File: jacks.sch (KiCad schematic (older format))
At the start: 71 parts, among them Q601 MMBT3904, Q602 MMBT3904, Q603 MMBT3904, Q604 MMBT3904, U601 MCP6004, U602 6N137

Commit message: only ground plane left
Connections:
- net GND: now also CVIN1.2, CVIN2.2, CVIN3.2, CVIN4.2
- no-connect marks 24 -> 20

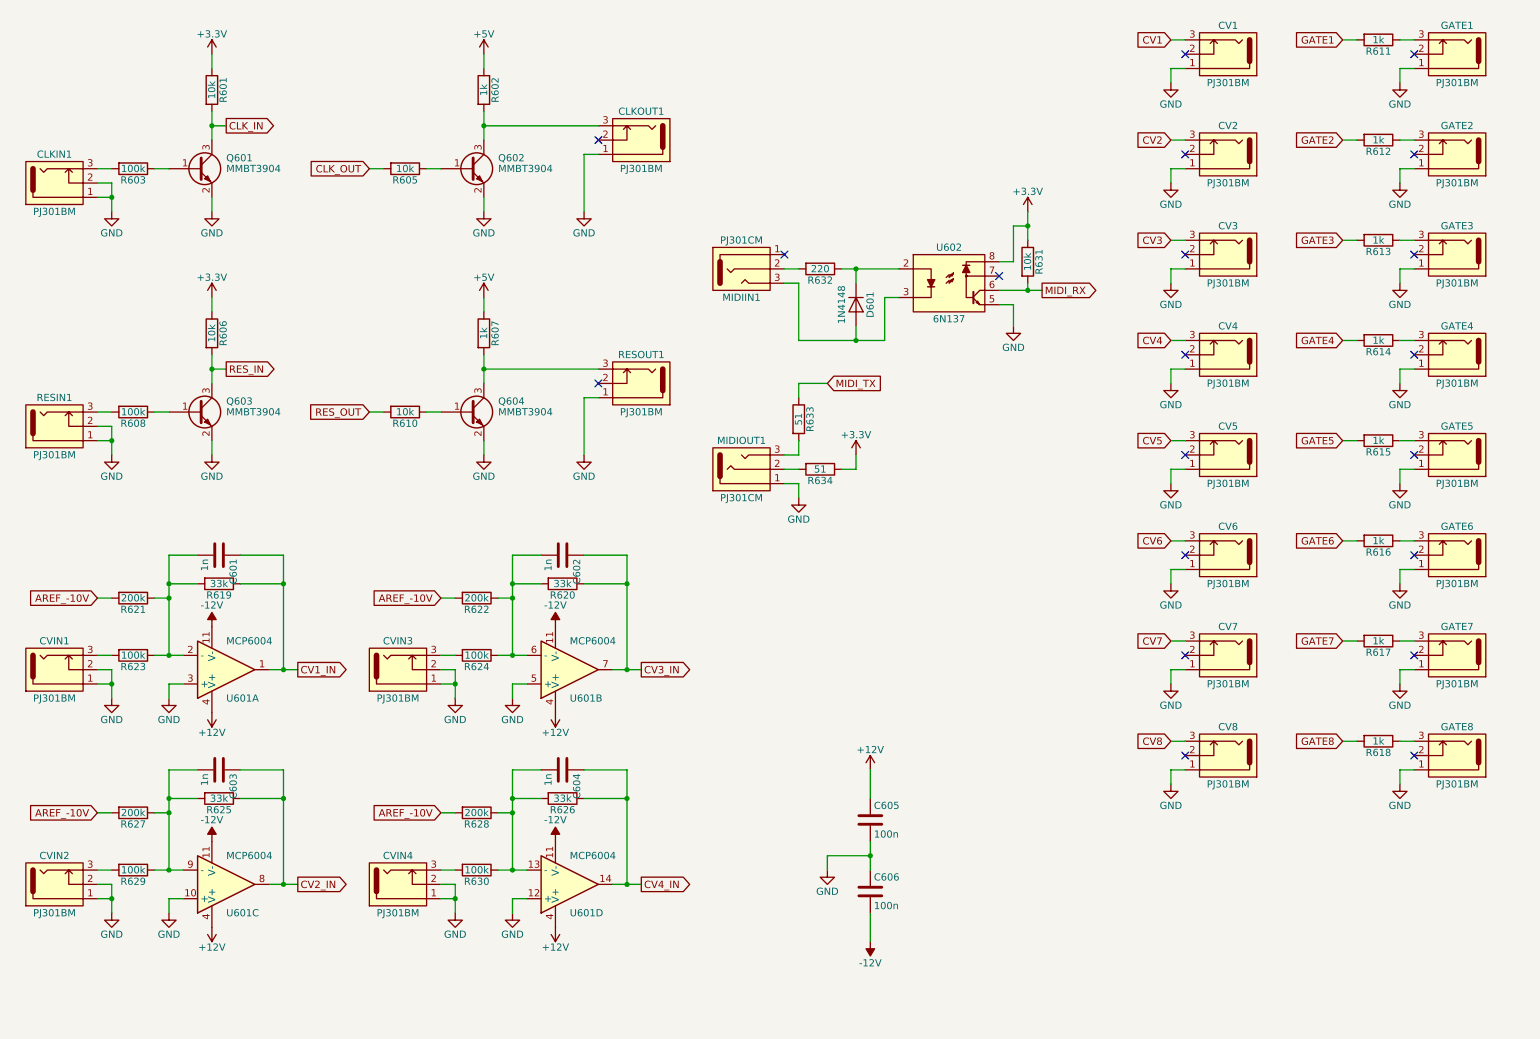
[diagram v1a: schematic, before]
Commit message: renamed jacks
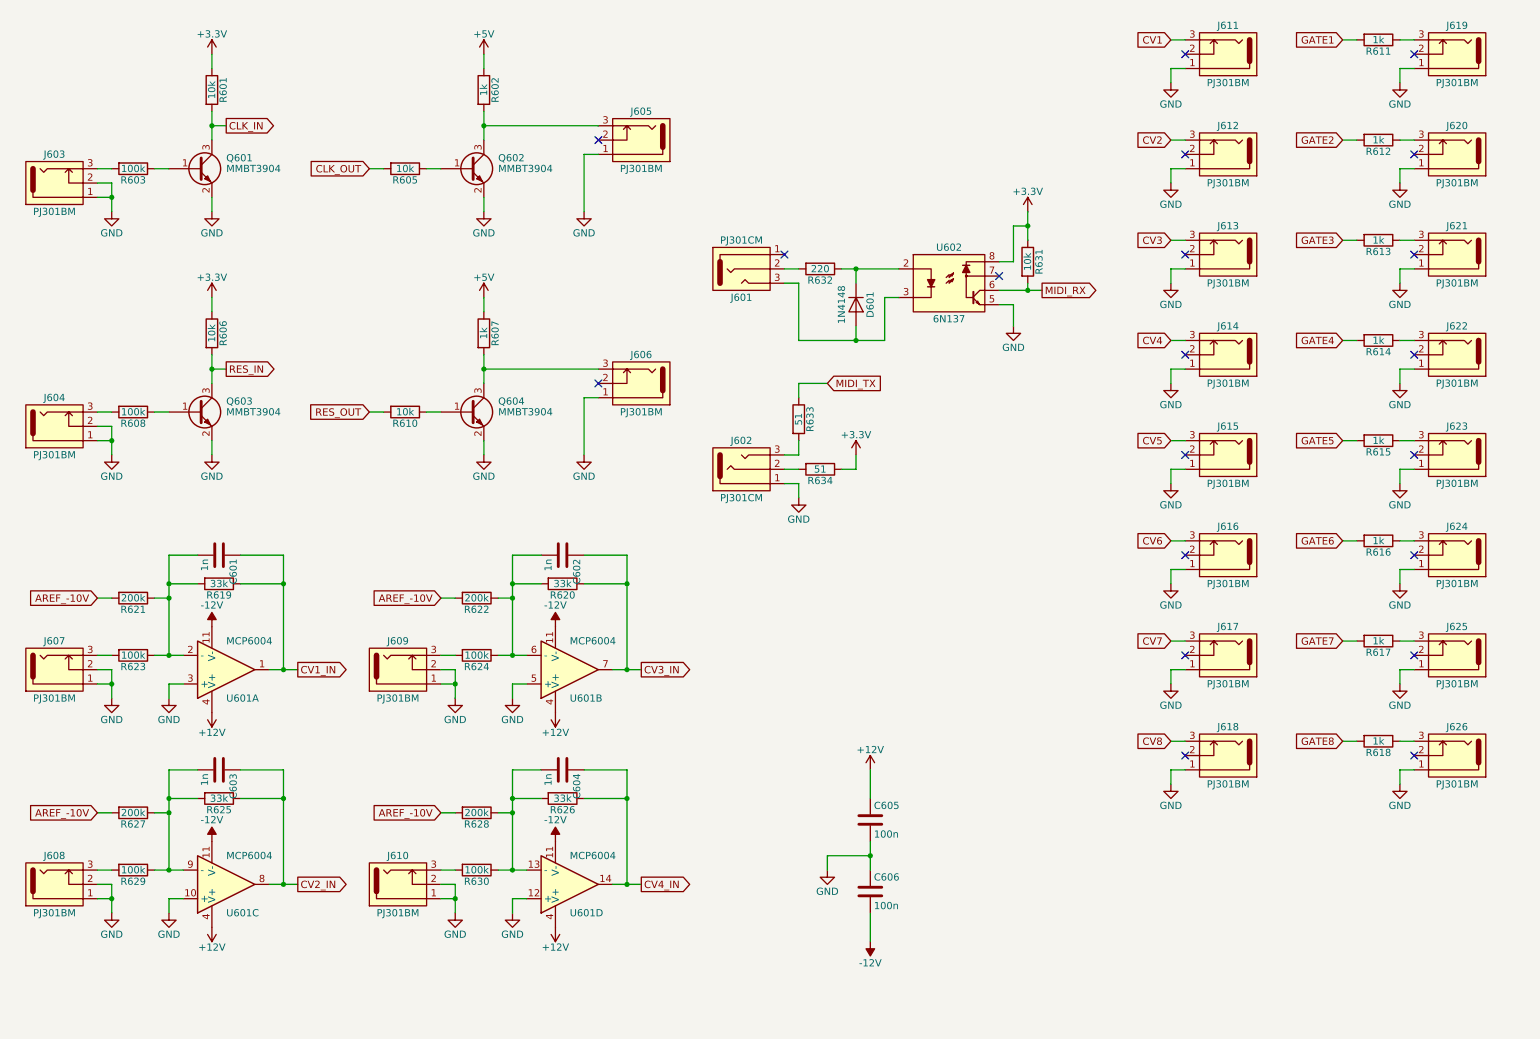
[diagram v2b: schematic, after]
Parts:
- renumbered MIDIIN1 to J601, MIDIOUT1 to J602, CLKIN1 to J603, RESIN1 to J604, CLKOUT1 to J605, RESOUT1 to J606, CVIN1 to J607, CVIN2 to J608, CVIN3 to J609, CVIN4 to J610, CV1 to J611, CV2 to J612, CV3 to J613, CV4 to J614, CV5 to J615, CV6 to J616, CV7 to J617, CV8 to J618, GATE1 to J619, GATE2 to J620, GATE3 to J621, GATE4 to J622, GATE5 to J623, GATE6 to J624, GATE7 to J625, GATE8 to J626
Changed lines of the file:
@@
 $EndComp
 $Comp
-L PJ301BM CLKIN1
+L PJ301BM J603
 U 1 1 59D9587D
 P 1000 1800
-F 0 "CLKIN1" H 800 1600 50  0000 C CNN
+F 0 "J603" H 800 1600 50  0000 C CNN
 F 1 "PJ301BM" H 800 2000 50  0000 C CNN
 F 2 "w_connector:PJ301BM" H 1150 1900 50  0001 C CNN
@@
 $EndComp
 $Comp
-L PJ301BM RESIN1
+L PJ301BM J604
 U 1 1 59D95DE7
 P 1000 3500
-F 0 "RESIN1" H 800 3300 50  0000 C CNN
+F 0 "J604" H 800 3300 50  0000 C CNN
 F 1 "PJ301BM" H 800 3700 50  0000 C CNN
 F 2 "w_connector:PJ301BM" H 1150 3600 50  0001 C CNN
@@
 $EndComp
 $Comp
-L PJ301BM CLKOUT1
+L PJ301BM J605
 U 1 1 59D96412
 P 4700 1500
-F 0 "CLKOUT1" H 4500 1300 50  0000 C CNN
+F 0 "J605" H 4500 1300 50  0000 C CNN
 F 1 "PJ301BM" H 4500 1700 50  0000 C CNN
 F 2 "w_connector:PJ301BM" H 4850 1600 50  0001 C CNN
@@
 $EndComp
 $Comp
-L PJ301BM RESOUT1
+L PJ301BM J606
 U 1 1 59D970A1
 P 4700 3200
-F 0 "RESOUT1" H 4500 3000 50  0000 C CNN
+F 0 "J606" H 4500 3000 50  0000 C CNN
 F 1 "PJ301BM" H 4500 3400 50  0000 C CNN
 F 2 "w_connector:PJ301BM" H 4850 3300 50  0001 C CNN
@@
 $EndComp
 $Comp
-L PJ301BM CV1
+L PJ301BM J611
 U 1 1 59D98BF9
 P 8800 900
-F 0 "CV1" H 8600 700 50  0000 C CNN
+F 0 "J611" H 8600 700 50  0000 C CNN
 F 1 "PJ301BM" H 8600 1100 50  0000 C CNN
 F 2 "w_connector:PJ301BM" H 8950 1000 50  0001 C CNN
@@
 $EndComp
 $Comp
-L PJ301BM CV2
+L PJ301BM J612
 U 1 1 59D99393
 P 8800 1600
-F 0 "CV2" H 8600 1400 50  0000 C CNN
+F 0 "J612" H 8600 1400 50  0000 C CNN
 F 1 "PJ301BM" H 8600 1800 50  0000 C CNN
 F 2 "w_connector:PJ301BM" H 8950 1700 50  0001 C CNN
@@
 $EndComp
 $Comp
-L PJ301BM CV3
+L PJ301BM J613
 U 1 1 59D99402
 P 8800 2300
-F 0 "CV3" H 8600 2100 50  0000 C CNN
+F 0 "J613" H 8600 2100 50  0000 C CNN
 F 1 "PJ301BM" H 8600 2500 50  0000 C CNN
 F 2 "w_connector:PJ301BM" H 8950 2400 50  0001 C CNN
@@
 $EndComp
 $Comp
-L PJ301BM CV4
+L PJ301BM J614
 U 1 1 59D99413
 P 8800 3000
-F 0 "CV4" H 8600 2800 50  0000 C CNN
+F 0 "J614" H 8600 2800 50  0000 C CNN
 F 1 "PJ301BM" H 8600 3200 50  0000 C CNN
 F 2 "w_connector:PJ301BM" H 8950 3100 50  0001 C CNN
@@
 $EndComp
 $Comp
-L PJ301BM CV5
+L PJ301BM J615
 U 1 1 59D9988E
 P 8800 3700
-F 0 "CV5" H 8600 3500 50  0000 C CNN
+F 0 "J615" H 8600 3500 50  0000 C CNN
 F 1 "PJ301BM" H 8600 3900 50  0000 C CNN
 F 2 "w_connector:PJ301BM" H 8950 3800 50  0001 C CNN
@@
 $EndComp
 $Comp
-L PJ301BM CV6
+L PJ301BM J616
 U 1 1 59D9989F
 P 8800 4400
-F 0 "CV6" H 8600 4200 50  0000 C CNN
+F 0 "J616" H 8600 4200 50  0000 C CNN
 F 1 "PJ301BM" H 8600 4600 50  0000 C CNN
 F 2 "w_connector:PJ301BM" H 8950 4500 50  0001 C CNN
@@
 $EndComp
 $Comp
-L PJ301BM CV7
+L PJ301BM J617
 U 1 1 59D998B0
 P 8800 5100
-F 0 "CV7" H 8600 4900 50  0000 C CNN
+F 0 "J617" H 8600 4900 50  0000 C CNN
 F 1 "PJ301BM" H 8600 5300 50  0000 C CNN
 F 2 "w_connector:PJ301BM" H 8950 5200 50  0001 C CNN
@@
 $EndComp
 $Comp
-L PJ301BM CV8
+L PJ301BM J618
 U 1 1 59D998C1
 P 8800 5800
-F 0 "CV8" H 8600 5600 50  0000 C CNN
+F 0 "J618" H 8600 5600 50  0000 C CNN
 F 1 "PJ301BM" H 8600 6000 50  0000 C CNN
 F 2 "w_connector:PJ301BM" H 8950 5900 50  0001 C CNN
@@
 $EndComp
 $Comp
-L PJ301BM GATE1
+L PJ301BM J619
 U 1 1 59D9C08F
 P 10400 900
-F 0 "GATE1" H 10200 700 50  0000 C CNN
+F 0 "J619" H 10200 700 50  0000 C CNN
 F 1 "PJ301BM" H 10200 1100 50  0000 C CNN
 F 2 "w_connector:PJ301BM" H 10550 1000 50  0001 C CNN
@@
 $EndComp
 $Comp
-L PJ301BM GATE2
+L PJ301BM J620
 U 1 1 59D9C0A0
 P 10400 1600
-F 0 "GATE2" H 10200 1400 50  0000 C CNN
+F 0 "J620" H 10200 1400 50  0000 C CNN
 F 1 "PJ301BM" H 10200 1800 50  0000 C CNN
 F 2 "w_connector:PJ301BM" H 10550 1700 50  0001 C CNN
@@
 $EndComp
 $Comp
-L PJ301BM GATE3
+L PJ301BM J621
 U 1 1 59D9C0B1
 P 10400 2300
-F 0 "GATE3" H 10200 2100 50  0000 C CNN
+F 0 "J621" H 10200 2100 50  0000 C CNN
 F 1 "PJ301BM" H 10200 2500 50  0000 C CNN
 F 2 "w_connector:PJ301BM" H 10550 2400 50  0001 C CNN
@@
 $EndComp
 $Comp
-L PJ301BM GATE4
+L PJ301BM J622
 U 1 1 59D9C0C2
 P 10400 3000
-F 0 "GATE4" H 10200 2800 50  0000 C CNN
+F 0 "J622" H 10200 2800 50  0000 C CNN
 F 1 "PJ301BM" H 10200 3200 50  0000 C CNN
 F 2 "w_connector:PJ301BM" H 10550 3100 50  0001 C CNN
@@
 $EndComp
 $Comp
-L PJ301BM GATE5
+L PJ301BM J623
 U 1 1 59D9C0D3
 P 10400 3700
-F 0 "GATE5" H 10200 3500 50  0000 C CNN
+F 0 "J623" H 10200 3500 50  0000 C CNN
 F 1 "PJ301BM" H 10200 3900 50  0000 C CNN
 F 2 "w_connector:PJ301BM" H 10550 3800 50  0001 C CNN
@@
 $EndComp
 $Comp
-L PJ301BM GATE6
+L PJ301BM J624
 U 1 1 59D9C0E4
 P 10400 4400
-F 0 "GATE6" H 10200 4200 50  0000 C CNN
+F 0 "J624" H 10200 4200 50  0000 C CNN
 F 1 "PJ301BM" H 10200 4600 50  0000 C CNN
 F 2 "w_connector:PJ301BM" H 10550 4500 50  0001 C CNN
@@
 $EndComp
 $Comp
-L PJ301BM GATE7
+L PJ301BM J625
 U 1 1 59D9C0F5
 P 10400 5100
-F 0 "GATE7" H 10200 4900 50  0000 C CNN
+F 0 "J625" H 10200 4900 50  0000 C CNN
 F 1 "PJ301BM" H 10200 5300 50  0000 C CNN
 F 2 "w_connector:PJ301BM" H 10550 5200 50  0001 C CNN
@@
 $EndComp
 $Comp
-L PJ301BM GATE8
+L PJ301BM J626
 U 1 1 59D9C106
 P 10400 5800
-F 0 "GATE8" H 10200 5600 50  0000 C CNN
+F 0 "J626" H 10200 5600 50  0000 C CNN
 F 1 "PJ301BM" H 10200 6000 50  0000 C CNN
 F 2 "w_connector:PJ301BM" H 10550 5900 50  0001 C CNN
@@
 $EndComp
 $Comp
-L PJ301BM CVIN1
+L PJ301BM J607
 U 1 1 59DF34A9
 P 1000 5200
-F 0 "CVIN1" H 800 5000 50  0000 C CNN
+F 0 "J607" H 800 5000 50  0000 C CNN
 F 1 "PJ301BM" H 800 5400 50  0000 C CNN
 F 2 "w_connector:PJ301BM" H 1150 5300 50  0001 C CNN
@@
 $EndComp
 $Comp
-L PJ301BM CVIN2
+L PJ301BM J608
 U 1 1 59DFAD0D
 P 1000 6700
-F 0 "CVIN2" H 800 6500 50  0000 C CNN
+F 0 "J608" H 800 6500 50  0000 C CNN
 F 1 "PJ301BM" H 800 6900 50  0000 C CNN
 F 2 "w_connector:PJ301BM" H 1150 6800 50  0001 C CNN
@@
 $EndComp
 $Comp
-L PJ301BM CVIN3
+L PJ301BM J609
 U 1 1 59DFB737
 P 3400 5200
-F 0 "CVIN3" H 3200 5000 50  0000 C CNN
+F 0 "J609" H 3200 5000 50  0000 C CNN
 F 1 "PJ301BM" H 3200 5400 50  0000 C CNN
 F 2 "w_connector:PJ301BM" H 3550 5300 50  0001 C CNN
@@
 $EndComp
 $Comp
-L PJ301BM CVIN4
+L PJ301BM J610
 U 1 1 59DFB784
 P 3400 6700
-F 0 "CVIN4" H 3200 6500 50  0000 C CNN
+F 0 "J610" H 3200 6500 50  0000 C CNN
 F 1 "PJ301BM" H 3200 6900 50  0000 C CNN
 F 2 "w_connector:PJ301BM" H 3550 6800 50  0001 C CNN
@@
 $EndComp
 $Comp
-L PJ301CM MIDIIN1
+L PJ301CM J601
 U 1 1 59DD452A
 P 5800 2400
-F 0 "MIDIIN1" H 5600 2200 50  0000 C CNN
+F 0 "J601" H 5600 2200 50  0000 C CNN
 F 1 "PJ301CM" H 5600 2600 50  0000 C CNN
 F 2 "w_connector:PJ301CM" H 5950 2500 50  0001 C CNN
@@
 $EndComp
 $Comp
-L PJ301CM MIDIOUT1
+L PJ301CM J602
 U 1 1 59DD4899
 P 5800 3800
-F 0 "MIDIOUT1" H 5600 3600 50  0000 C CNN
+F 0 "J602" H 5600 3600 50  0000 C CNN
 F 1 "PJ301CM" H 5600 4000 50  0000 C CNN
 F 2 "w_connector:PJ301CM" H 5950 3900 50  0001 C CNN

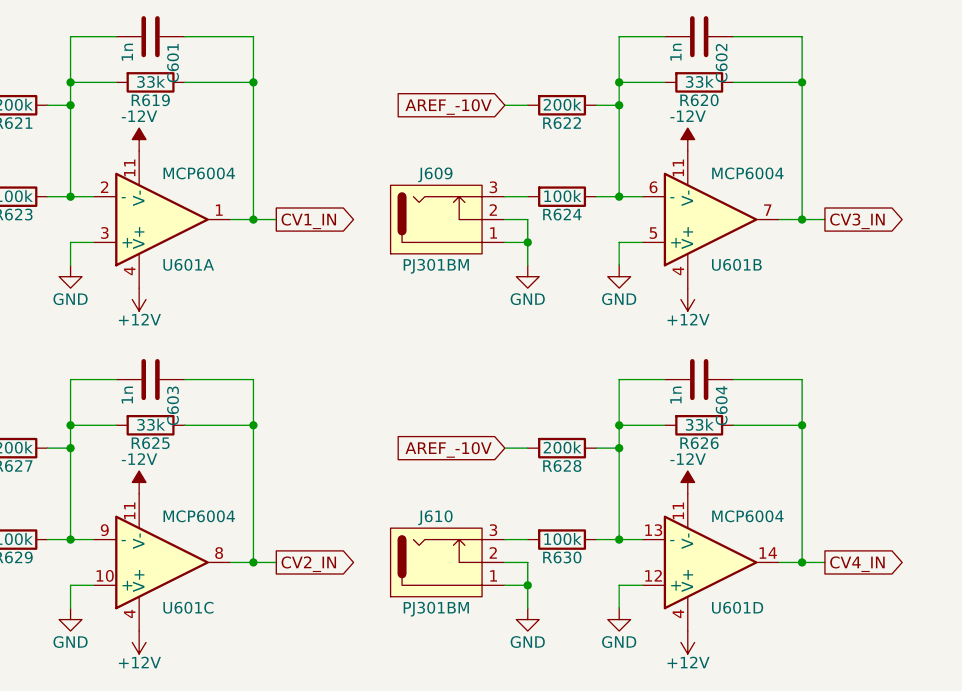
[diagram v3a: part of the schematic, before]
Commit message: replaced MCP6004 with TL074
Fixes #1
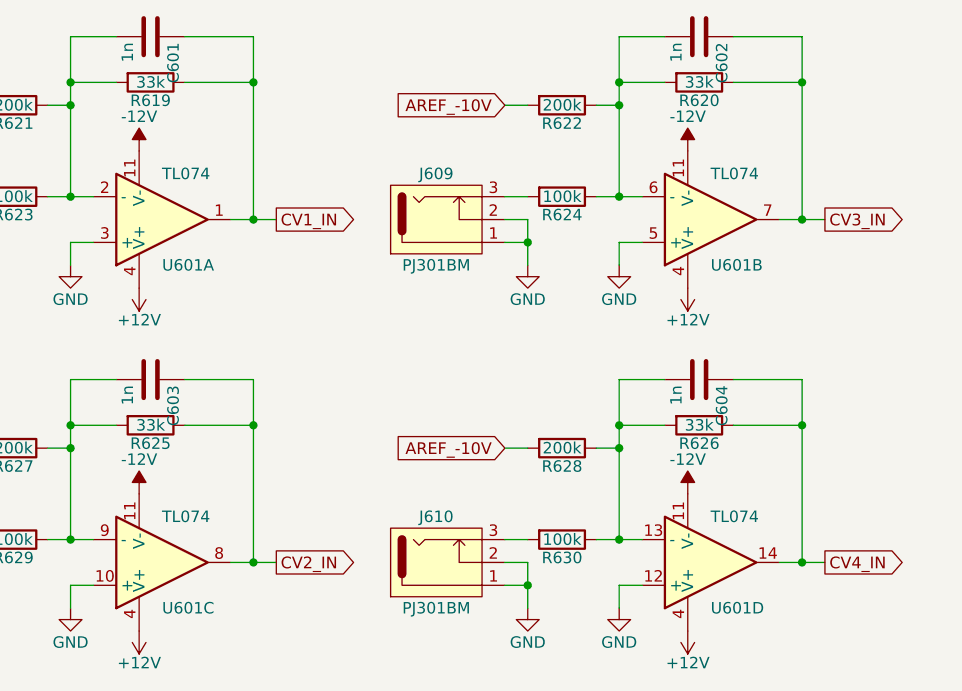
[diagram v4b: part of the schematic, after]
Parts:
- U601: value MCP6004 -> TL074; MFN Microchip -> Texas Instruments; MFP MCP6004-I/SL -> TL074CD
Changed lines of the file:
@@
 P 2000 5200
 F 0 "U601" H 2000 5400 50  0000 L CNN
-F 1 "MCP6004" H 2000 5000 50  0000 L CNN
+F 1 "TL074" H 2000 5000 50  0000 L CNN
 F 2 "Housings_SOIC:SOIC-14_3.9x8.7mm_Pitch1.27mm" H 1950 5300 50  0001 C CNN
-F 3 "http://datasheet.octopart.com/MCP6004-I/SL-Microchip-datasheet-8823409.pdf" H 2050 5400 50  0001 C CNN
-F 4 "Microchip" H 2000 5500 50  0001 C CNN "MFN"
-F 5 "MCP6004-I/SL" H 2000 5500 50  0001 C CNN "MFP"
+F 3 "https://octopart.com/click/track?ct=datasheets&hlid=24928135&ppid=93637&sid=370&sig=0014035" H 2050 5400 50  0001 C CNN
+F 4 "Texas Instruments" H 2000 5500 50  0001 C CNN "MFN"
+F 5 "TL074CD" H 2000 5500 50  0001 C CNN "MFP"
 	1    2000 5200
 	1    0    0    1
@@
 P 2000 6700
 F 0 "U601" H 2000 6900 50  0000 L CNN
-F 1 "MCP6004" H 2000 6500 50  0000 L CNN
+F 1 "TL074" H 2000 6500 50  0000 L CNN
 F 2 "Housings_SOIC:SOIC-14_3.9x8.7mm_Pitch1.27mm" H 1950 6800 50  0001 C CNN
-F 3 "http://datasheet.octopart.com/MCP6004-I/SL-Microchip-datasheet-8823409.pdf" H 2050 6900 50  0001 C CNN
-F 4 "Microchip" H 2000 7000 50  0001 C CNN "MFN"
-F 5 "MCP6004-I/SL" H 2000 7000 50  0001 C CNN "MFP"
+F 3 "https://octopart.com/click/track?ct=datasheets&hlid=24928135&ppid=93637&sid=370&sig=0014035" H 2050 6900 50  0001 C CNN
+F 4 "Texas Instruments" H 2000 7000 50  0001 C CNN "MFN"
+F 5 "TL074CD" H 2000 7000 50  0001 C CNN "MFP"
 	3    2000 6700
 	1    0    0    1
@@
 P 4400 5200
 F 0 "U601" H 4400 5400 50  0000 L CNN
-F 1 "MCP6004" H 4400 5000 50  0000 L CNN
+F 1 "TL074" H 4400 5000 50  0000 L CNN
 F 2 "Housings_SOIC:SOIC-14_3.9x8.7mm_Pitch1.27mm" H 4350 5300 50  0001 C CNN
-F 3 "http://datasheet.octopart.com/MCP6004-I/SL-Microchip-datasheet-8823409.pdf" H 4450 5400 50  0001 C CNN
-F 4 "Microchip" H 4400 5500 50  0001 C CNN "MFN"
-F 5 "MCP6004-I/SL" H 4400 5500 50  0001 C CNN "MFP"
+F 3 "https://octopart.com/click/track?ct=datasheets&hlid=24928135&ppid=93637&sid=370&sig=0014035" H 4450 5400 50  0001 C CNN
+F 4 "Texas Instruments" H 4400 5500 50  0001 C CNN "MFN"
+F 5 "TL074CD" H 4400 5500 50  0001 C CNN "MFP"
 	2    4400 5200
 	1    0    0    1
@@
 P 4400 6700
 F 0 "U601" H 4400 6900 50  0000 L CNN
-F 1 "MCP6004" H 4400 6500 50  0000 L CNN
+F 1 "TL074" H 4400 6500 50  0000 L CNN
 F 2 "Housings_SOIC:SOIC-14_3.9x8.7mm_Pitch1.27mm" H 4350 6800 50  0001 C CNN
-F 3 "http://datasheet.octopart.com/MCP6004-I/SL-Microchip-datasheet-8823409.pdf" H 4450 6900 50  0001 C CNN
-F 4 "Microchip" H 4400 7000 50  0001 C CNN "MFN"
-F 5 "MCP6004-I/SL" H 4400 7000 50  0001 C CNN "MFP"
+F 3 "https://octopart.com/click/track?ct=datasheets&hlid=24928135&ppid=93637&sid=370&sig=0014035" H 4450 6900 50  0001 C CNN
+F 4 "Texas Instruments" H 4400 7000 50  0001 C CNN "MFN"
+F 5 "TL074CD" H 4400 7000 50  0001 C CNN "MFP"
 	4    4400 6700
 	1    0    0    1

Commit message: work in progress
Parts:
- added U603: 74LV1T34, symbol 74LV1T34
- C601, C602, C603, C604, C605, C606: footprint Capacitors_SMD:C_0603 -> Capacitors_SMD:C_0603_HandSoldering
- R601, R602, R603, R605, R606, R607, R608, R610, R611, R612, R613, R614, R615, R616, R617, R618, R619, R620, R621, R622, R623, R624, R625, R626, R627, R628, R629, R630, R631, R632: footprint Resistors_SMD:R_0603 -> Resistors_SMD:R_0603_HandSoldering
- R633, R634: value 51 -> 220; footprint Resistors_SMD:R_0603 -> Resistors_SMD:R_0603_HandSoldering
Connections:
- net +3V3: no longer R634.1
- net +5V: now also R634.1, U603.5 (VCC)
- net GND: now also U603.3 (GND)
- net MIDI_TX: now also U603.2 (A); no longer R633.1
- new net: R633.1, U603.4 (Y)
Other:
- note added: "CLOCK INPUTS"
- note added: "CLOCK OUTPUTS"
- note added: "CV INPUTS"
- note added: "CV OUTPUTS"
- note added: "GATE OUTPUTS"
- note added: "MIDI"
- note added: "NEW"
- moved on the sheet: C601, C602, C603, C604, C605, C606, D601, J601, J602, J603, J604, J605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

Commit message: work in progress
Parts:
- U602: value 6N137 -> VO0600T; footprint Housings_DIP:SMDIP-8_W9.53mm -> Housings_SOIC:SOIC-8_3.9x4.9mm_Pitch1.27mm; MFN Lite-On -> Vishay; MFP 6N137S -> VO0600T
- U603: footprint (none) -> TO_SOT_Packages_SMD:SOT-23-5; MFN (none) -> Texas Instruments; MFP (none) -> SN74LV1T34DBVR

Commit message: work in progress
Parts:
- C601, C602, C603, C604, C605, C606: footprint Capacitors_SMD:C_0603_HandSoldering -> w_capacitor:C_0603
- R601, R602, R603, R605, R606, R607, R608, R610, R611, R612, R613, R614, R615, R616, R617, R618, R619, R620, R621, R622, R623, R624, R625, R626, R627, R628, R629, R630, R631, R632, R633, R634: footprint Resistors_SMD:R_0603_HandSoldering -> w_resistor:R_0603

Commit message: cleanup
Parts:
- D601: footprint Diodes_SMD:D_SOD-123 -> w_diode:D_SOD-123
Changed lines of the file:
@@
 F 0 "D601" H 6600 1850 50  0000 C CNN
 F 1 "1N4148" H 6600 1650 50  0000 C CNN
-F 2 "Diodes_SMD:D_SOD-123" H 6600 1750 50  0001 C CNN
+F 2 "w_diode:D_SOD-123" H 6600 1750 50  0001 C CNN
 F 3 "http://datasheet.octopart.com/1N4148W-7-F-Diodes-Inc.-datasheet-12518151.pdf" H 6600 1750 50  0001 C CNN
 F 4 "Diodes Inc." H 6600 1950 50  0001 C CNN "MFN"
